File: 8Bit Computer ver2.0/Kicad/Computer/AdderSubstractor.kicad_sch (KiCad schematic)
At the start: 15 parts, among them IC183 SN74LVC1G14DBVR, IC184 SN74ABT245BDWR, IC185 SN74HCS4075DR, IC186 SN74LVC1G08DBVR, IC187 SN74AHC86DR, IC188 SN74AHC86DR, IC189 SN74AHC74DR, IC190 SN74LVC1G32DBVR, IC191 SN74F283D, IC192 SN74F283D, IC193 SN74F283D, IC194 SN74LVC1G86DBVR, IC195 SN74ABT574ADWR, IC196 SN74ABT574ADWR, IC197 SN74LVC1G14DBVR

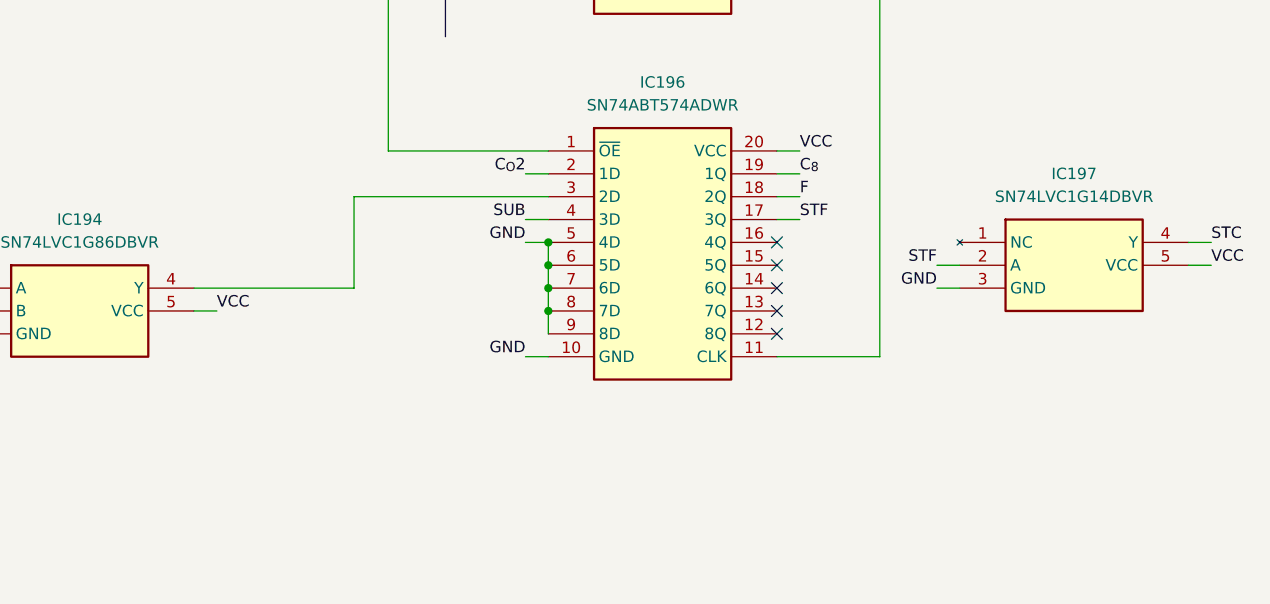
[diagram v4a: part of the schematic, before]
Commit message: Kicad, parts
parts:
added Mux 4:1 for CLK
added LM555
Kicad:
added some Diodes for Flash disable
fixed wrong routing of flag register
fixed wrong routing of STC STF in INC/AddS
LM555 circuit for 1Hz to 100Hz
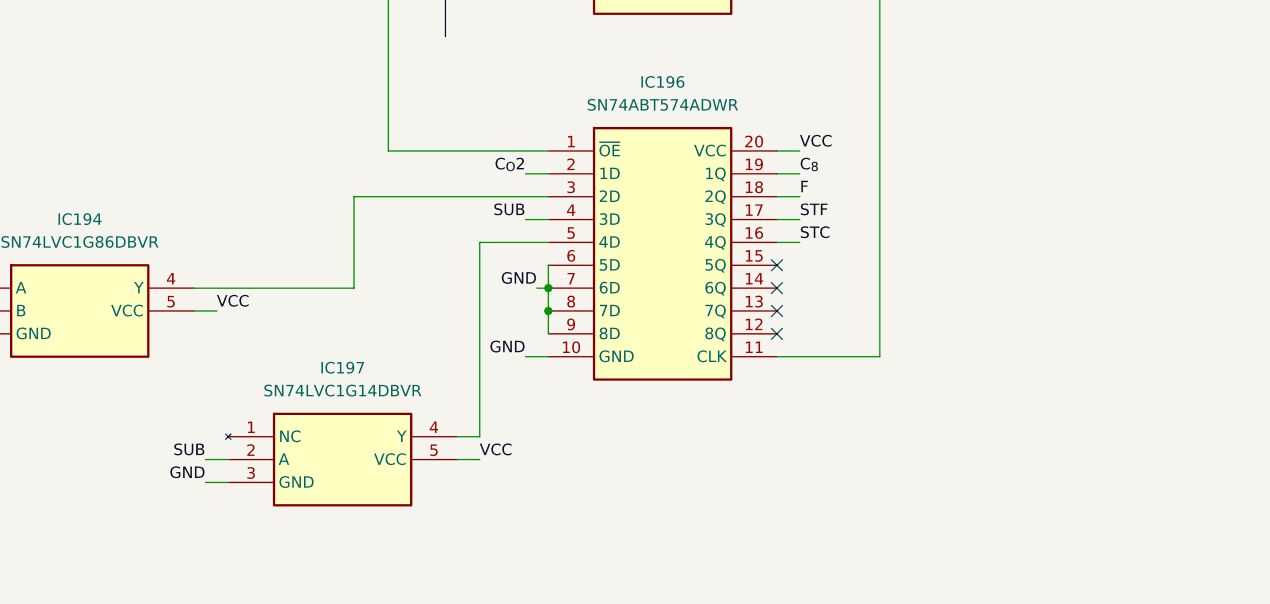
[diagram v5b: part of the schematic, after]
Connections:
- net GND: no longer IC196.5 (4D)
- net STC: now also IC196.16 (4Q); no longer IC197.4 (Y)
- net STF: no longer IC197.2 (A)
- net SUB: now also IC197.2 (A)
- new net: IC196.5 (4D), IC197.4 (Y)
- no-connect marks 13 -> 12
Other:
- moved on the sheet: IC197
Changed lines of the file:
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@@
 	(paper "A3")
 	(junction
-		(at 327.66 107.95)
-		(diameter 0)
-		(color 0 0 0 0)
-	)
-	(junction
 		(at 309.88 45.72)
 		(diameter 0)
@@
 	)
 	(junction
-		(at 327.66 110.49)
-		(diameter 0)
-		(color 0 0 0 0)
-	)
-	(junction
 		(at 81.28 35.56)
 		(diameter 0)
@@
 	)
 	(no_connect
-		(at 353.06 107.95)
-	)
-	(no_connect
 		(at 243.84 107.95)
 	)
@@
 	(wire
 		(pts
-			(xy 398.78 107.95) (xy 401.32 107.95)
+			(xy 317.5 129.54) (xy 320.04 129.54)
 		)
 		(stroke
@@
 	(wire
 		(pts
-			(xy 325.12 107.95) (xy 327.66 107.95)
-		)
-		(stroke
-			(width 0)
-			(type default)
-		)
-	)
-	(wire
-		(pts
 			(xy 256.54 92.71) (xy 243.84 92.71)
 		)
@@
 	(wire
 		(pts
+			(xy 320.04 129.54) (xy 320.04 107.95)
+		)
+		(stroke
+			(width 0)
+			(type default)
+		)
+	)
+	(wire
+		(pts
 			(xy 318.77 59.69) (xy 327.66 59.69)
 		)
@@
 	(wire
 		(pts
-			(xy 398.78 110.49) (xy 401.32 110.49)
+			(xy 317.5 132.08) (xy 320.04 132.08)
 		)
 		(stroke
@@
 	(wire
 		(pts
+			(xy 353.06 107.95) (xy 355.6 107.95)
+		)
+		(stroke
+			(width 0)
+			(type default)
+		)
+	)
+	(wire
+		(pts
 			(xy 31.75 119.38) (xy 39.37 119.38)
 		)
@@
 		)
 	)
+	(wire
+		(pts
+			(xy 326.39 113.03) (xy 327.66 113.03)
+		)
+		(stroke
+			(width 0)
+			(type default)
+		)
+	)
 	(bus
 		(pts
@@
 	(wire
 		(pts
-			(xy 370.84 113.03) (xy 373.38 113.03)
+			(xy 289.56 134.62) (xy 292.1 134.62)
 		)
 		(stroke
@@
 		)
 	)
-	(wire
-		(pts
-			(xy 327.66 107.95) (xy 327.66 110.49)
-		)
-		(stroke
-			(width 0)
-			(type default)
-		)
-	)
 	(bus
 		(pts
@@
 	(wire
 		(pts
-			(xy 370.84 110.49) (xy 373.38 110.49)
+			(xy 289.56 132.08) (xy 292.1 132.08)
 		)
 		(stroke
@@
 	(wire
 		(pts
+			(xy 320.04 107.95) (xy 327.66 107.95)
+		)
+		(stroke
+			(width 0)
+			(type default)
+		)
+	)
+	(wire
+		(pts
 			(xy 205.74 67.31) (xy 218.44 67.31)
 		)
@@
 		)
 	)
+	(label "STC"
+		(at 355.6 107.95 0)
+		(effects
+			(font
+				(size 1.27 1.27)
+			)
+			(justify left bottom)
+		)
+	)
 	(label "GND"
 		(at 132.08 48.26 180)
@@
 		)
 	)
-	(label "STC"
-		(at 401.32 107.95 0)
-		(effects
-			(font
-				(size 1.27 1.27)
-			)
-			(justify left bottom)
-		)
-	)
 	(label "Sum2"
 		(at 325.12 64.77 180)
@@
 		)
 	)
+	(label "GND"
+		(at 326.39 113.03 180)
+		(effects
+			(font
+				(size 1.27 1.27)
+			)
+			(justify right bottom)
+		)
+	)
 	(label "B7"
 		(at 151.13 138.43 0)
@@
 	)
 	(label "VCC"
-		(at 401.32 110.49 0)
+		(at 320.04 132.08 0)
 		(effects
 			(font
@@
 		)
 	)
-	(label "STF"
-		(at 370.84 110.49 180)
-		(effects
-			(font
-				(size 1.27 1.27)
-			)
-			(justify right bottom)
-		)
-	)
 	(label "VCC"
 		(at 132.08 33.02 180)
@@
 	)
 	(label "GND"
-		(at 370.84 113.03 180)
+		(at 289.56 134.62 180)
 		(effects
 			(font
@@
 		)
 	)
+	(label "SUB"
+		(at 289.56 132.08 180)
+		(effects
+			(font
+				(size 1.27 1.27)
+			)
+			(justify right bottom)
+		)
+	)
 	(label "C_{in}"
 		(at 102.87 67.31 180)
@@
 	)
 	(label "GND"
-		(at 325.12 107.95 180)
-		(effects
-			(font
-				(size 1.27 1.27)
-			)
-			(justify right bottom)
-		)
-	)
-	(label "GND"
 		(at 246.38 123.19 0)
 		(effects
@@
 	(symbol
 		(lib_id "Samacsys:SN74LVC1G14DBVR")
-		(at 373.38 107.95 0)
+		(at 292.1 129.54 0)
 		(unit 1)
 		(exclude_from_sim no)
@@
 		(fields_autoplaced yes)
 		(property "Reference" "IC197"
-			(at 386.08 100.33 0)
+			(at 304.8 121.92 0)
 			(effects
 				(font
@@
 		)
 		(property "Value" "SN74LVC1G14DBVR"
-			(at 386.08 102.87 0)
+			(at 304.8 124.46 0)
 			(effects
 				(font
@@
 		)
 		(property "Footprint" "Samacsys:SOT95P280X145-5N"
-			(at 394.97 202.87 0)
+			(at 313.69 224.46 0)
 			(effects
 				(font
@@
 		)
 		(property "Datasheet" "https://datasheet.datasheetarchive.com/originals/distributors/Datasheets-DGA13/1136296.pdf"
-			(at 394.97 302.87 0)
+			(at 313.69 324.46 0)
 			(effects
 				(font
@@
 		)
 		(property "Description" "TEXAS INSTRUMENTS - SN74LVC1G14DBVR - IC, SCHMITT TRIGGER INVERTER, SMD"
-			(at 373.38 107.95 0)
+			(at 292.1 129.54 0)
 			(effects
 				(font
@@
 		)
 		(property "Height" "1.45"
-			(at 394.97 502.87 0)
+			(at 313.69 524.46 0)
 			(effects
 				(font
@@
 		)
 		(property "Mouser Part Number" "595-SN74LVC1G14DBVR"
-			(at 394.97 602.87 0)
+			(at 313.69 624.46 0)
 			(effects
 				(font
@@
 		)
 		(property "Mouser Price/Stock" "https://www.mouser.co.uk/ProductDetail/Texas-Instruments/SN74LVC1G14DBVR?qs=dT9u2OTAaVWRIgCrQFnxuQ%3D%3D"
-			(at 394.97 702.87 0)
+			(at 313.69 724.46 0)
 			(effects
 				(font
@@
 		)
 		(property "Manufacturer_Name" "Texas Instruments"
-			(at 394.97 802.87 0)
+			(at 313.69 824.46 0)
 			(effects
 				(font
@@
 		)
 		(property "Manufacturer_Part_Number" "SN74LVC1G14DBVR"
-			(at 394.97 902.87 0)
+			(at 313.69 924.46 0)
 			(effects
 				(font

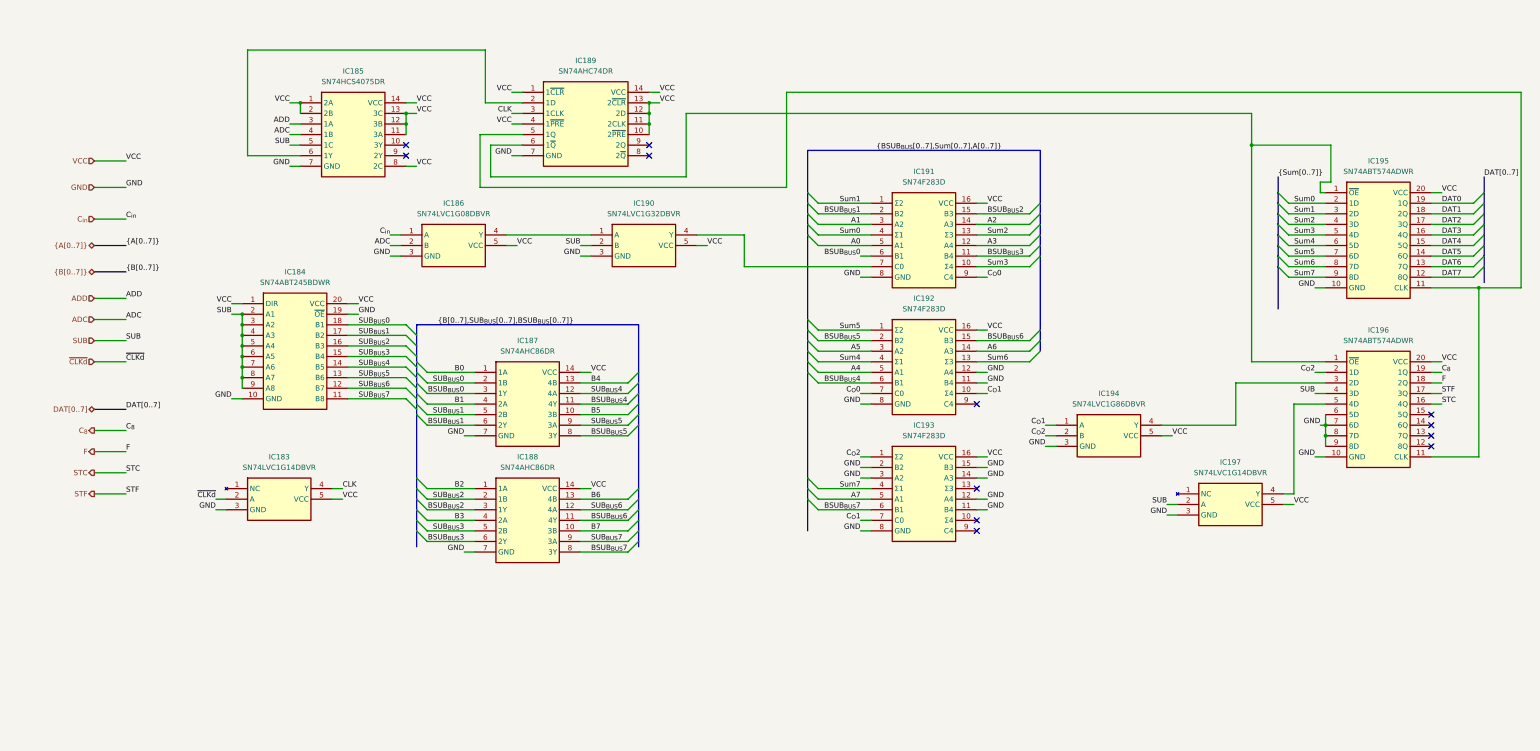
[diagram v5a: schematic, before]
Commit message: part 1 of changing to A4
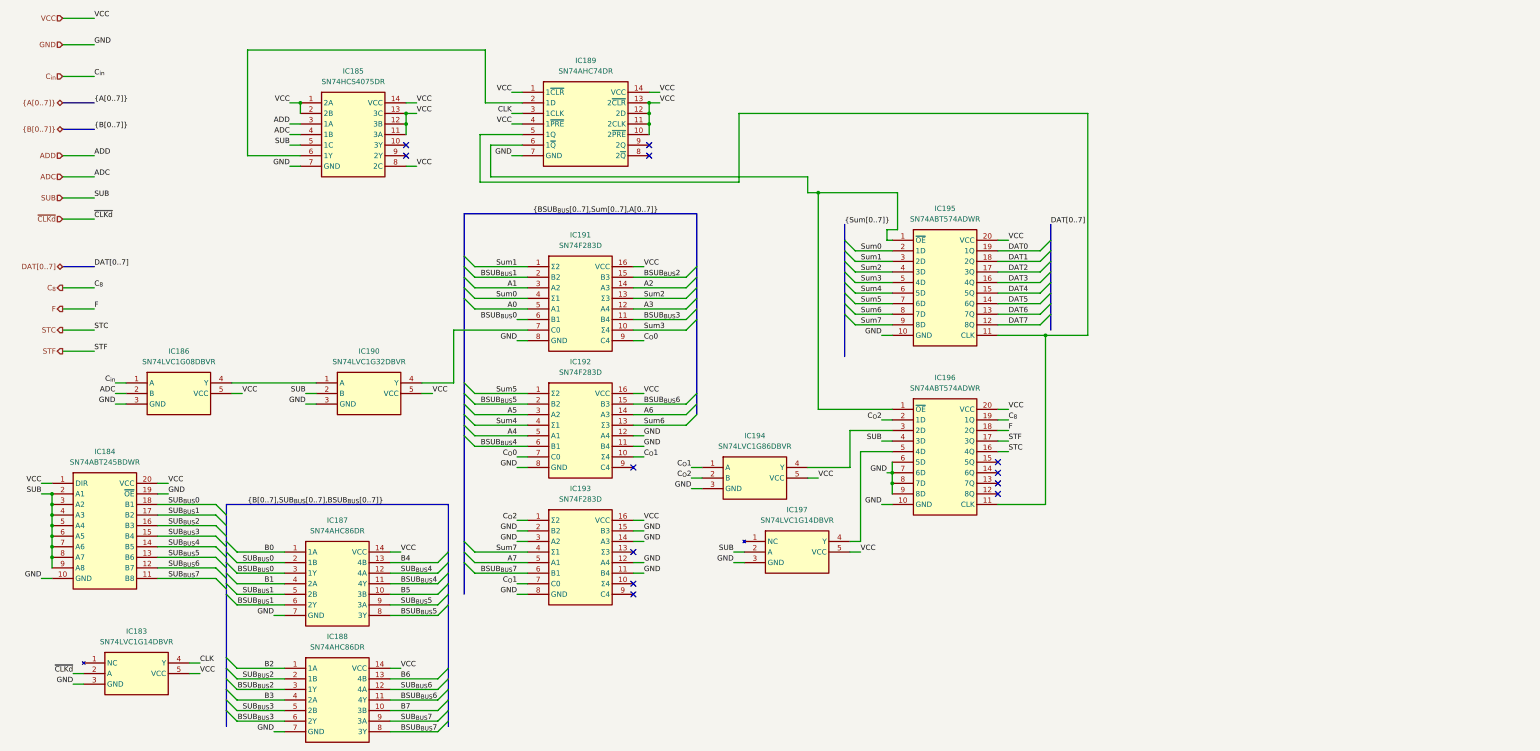
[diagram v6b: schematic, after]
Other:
- moved on the sheet: IC183, IC184, IC186, IC187, IC188, IC190, IC191, IC192, IC193, IC194, IC195, IC196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

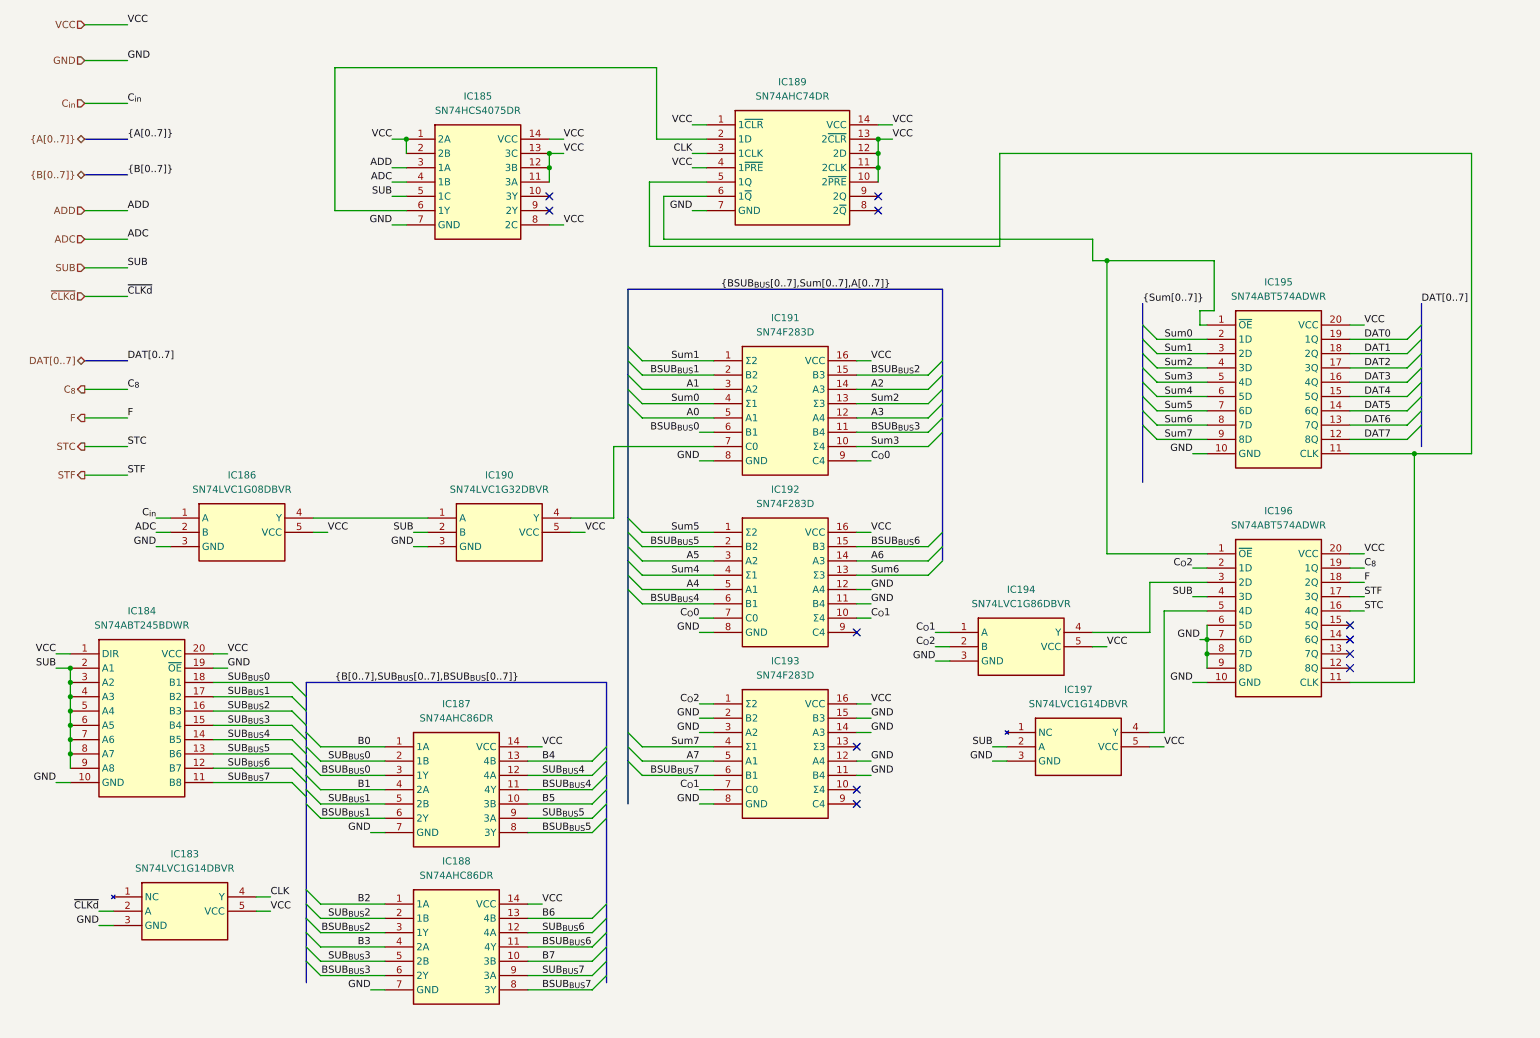
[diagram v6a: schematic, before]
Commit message: changed page numbers, compressed ROOT file from A1 to A4
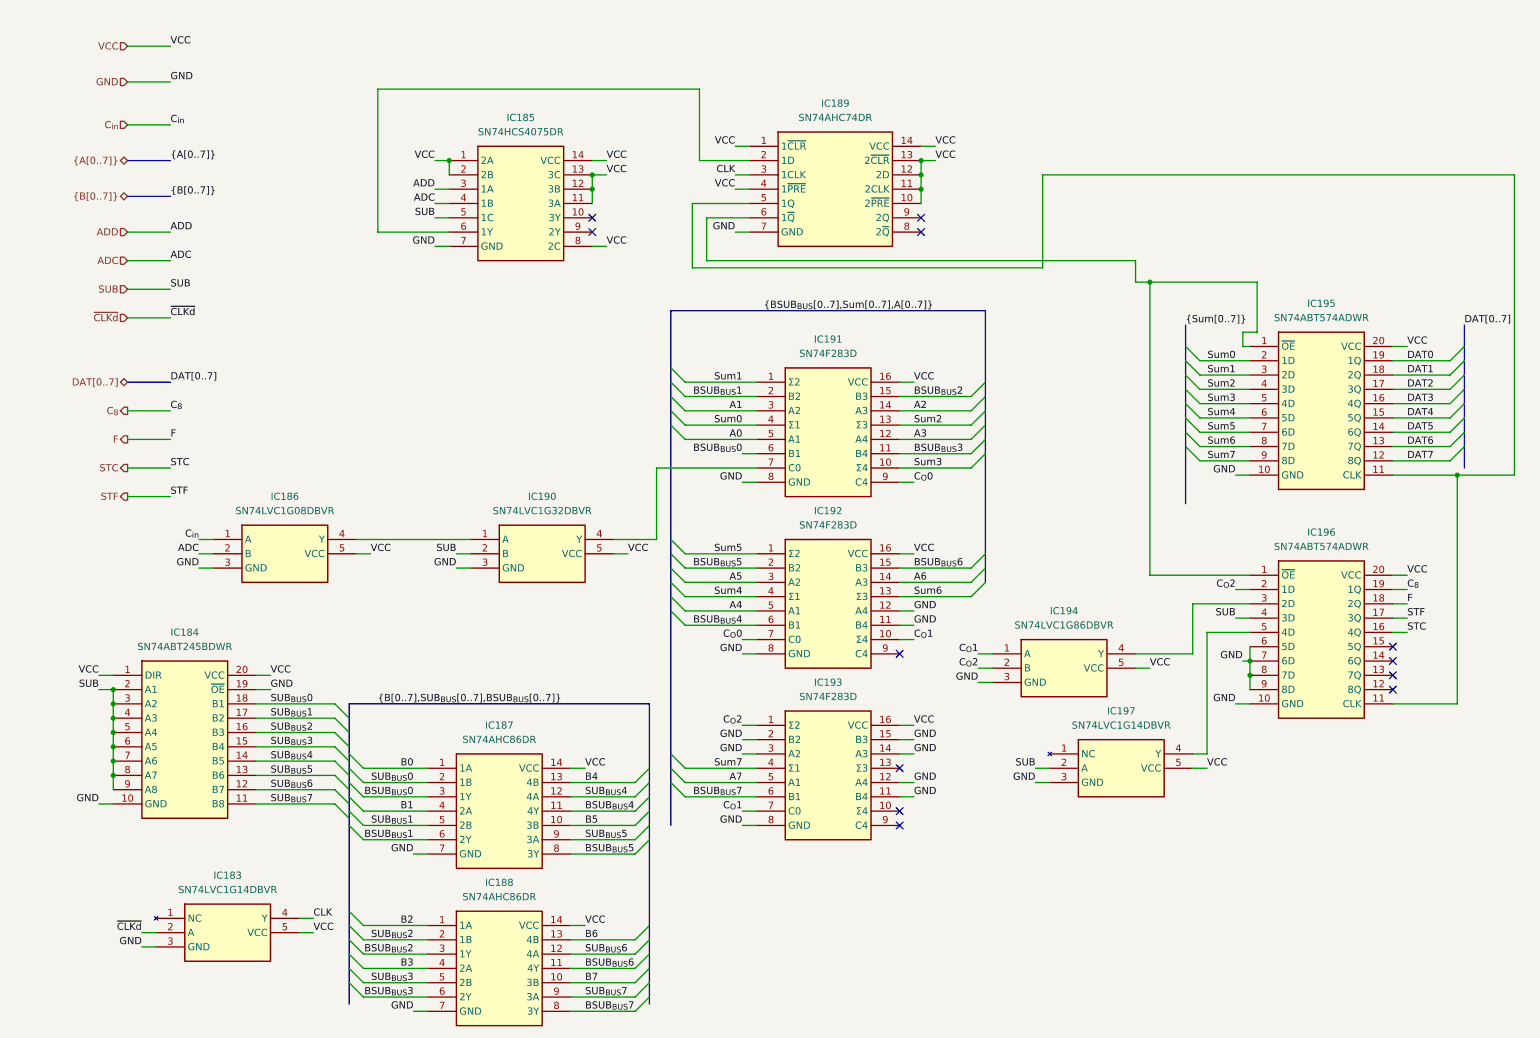
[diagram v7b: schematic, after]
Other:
- moved on the sheet: IC183, IC184, IC185, IC186, IC187, IC188, IC189, IC190, IC191, IC192, IC193, IC194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

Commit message: changed page numbers, every schematic is now A4
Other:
- title: (none) -> ${SHEETNAME}
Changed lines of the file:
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@@
 	(generator_version "9.0")
 	(paper "A4")
+	(title_block
+		(title "${SHEETNAME}")
+		(date "2026-03-21")
+		(rev "2.7")
+	)
 	(junction
 		(at 172.72 39.37)
